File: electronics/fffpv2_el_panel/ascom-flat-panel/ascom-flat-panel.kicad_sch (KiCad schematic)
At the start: 17 parts, among them J1 Servo, J2 Conn_01x02, Q1 IRLZ34N, U1 XIAO-SAMD21-DIP, U2 TLC272, U4 LM317_TO-220

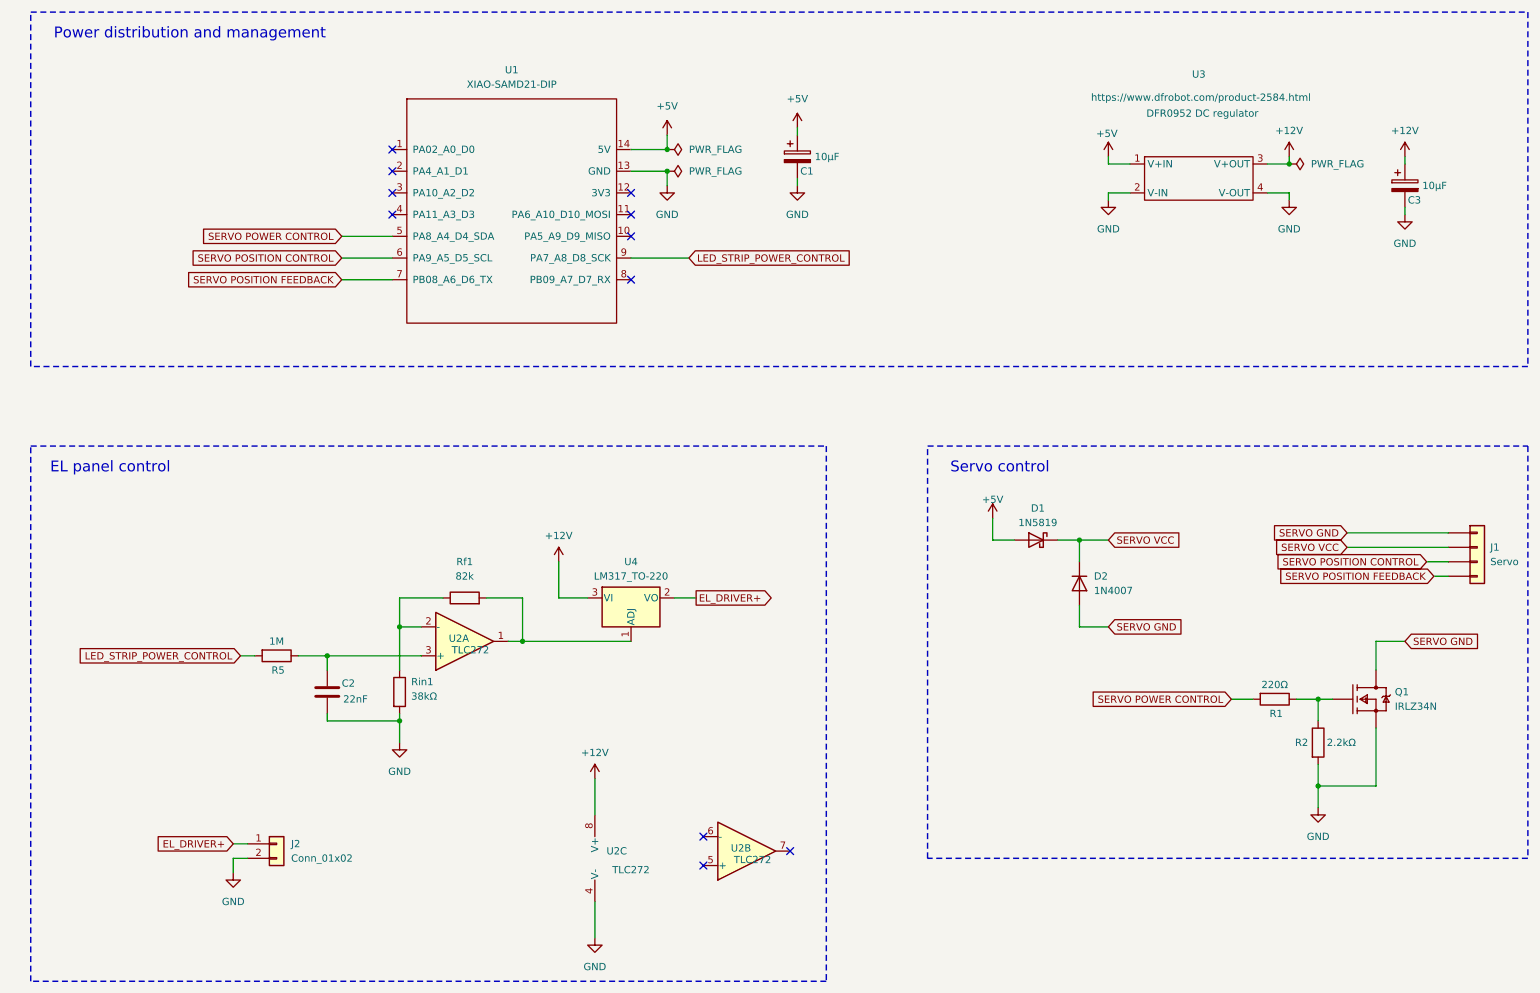
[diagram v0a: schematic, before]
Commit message: Updatong shcematics and PCB to use DAC for EL driver PWR ctrl
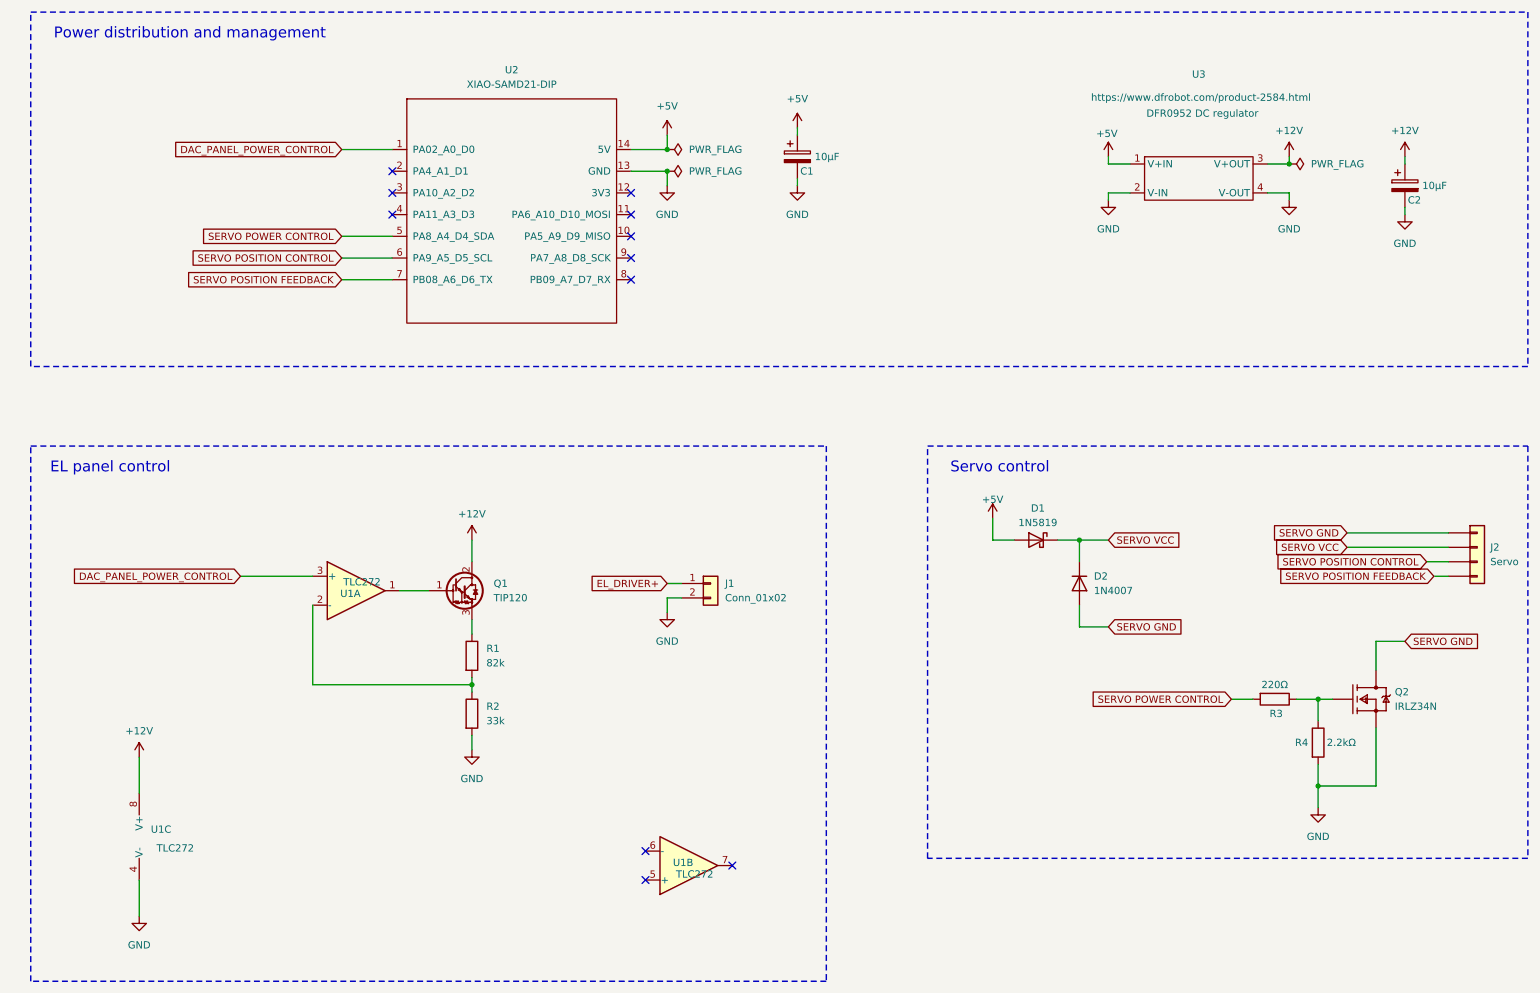
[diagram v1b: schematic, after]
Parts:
- removed C2: 22nF, Capacitor_THT:C_Disc_D3.0mm_W1.6mm_P2.50mm, symbol Device:C
- removed R5: 1M, Resistor_THT:R_Axial_DIN0207_L6.3mm_D2.5mm_P10.16mm_Horizontal, symbol Device:R
- removed Rf1: 82k, Resistor_THT:R_Axial_DIN0207_L6.3mm_D2.5mm_P10.16mm_Horizontal, symbol Device:R
- removed Rin1: 38kΩ, Resistor_THT:R_Axial_DIN0207_L6.3mm_D2.5mm_P10.16mm_Horizontal, symbol Device:R
- removed U4: LM317_TO-220, Package_TO_SOT_THT:TO-220-3_Vertical, symbol Regulator_Linear:LM317_TO-220
- added Q1: TIP120, Package_TO_SOT_THT:TO-220-3_Vertical, symbol Transistor_BJT:TIP120
- added R1: 82k, Resistor_THT:R_Axial_DIN0207_L6.3mm_D2.5mm_P10.16mm_Horizontal, symbol Device:R
- added R2: 33k, Resistor_THT:R_Axial_DIN0207_L6.3mm_D2.5mm_P10.16mm_Horizontal, symbol Device:R
- renumbered C3 to C2, J2 to J1, J1 to J2, Q1 to Q2, R1 to R3, R2 to R4, U2 to U1, U1 to U2
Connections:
- net +12V: now also Q1.2 (C)
- net GND: now also R2.2
- net at U1.1: now also Q1.1 (B)
- net DAC_PANEL_POWER_CONTROL: now reaches U1.3 (+)
- net DAC_PANEL_POWER_CONTROL: now also U2.1 (PA02_A0_D0)
- net at U1.2 (-): now also R1.2, R2.1
- net LED_STRIP_POWER_CONTROL: no longer names the net of U2.9 (PA7_A8_D8_SCK)
- new net: Q1.3 (E), R1.1
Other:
- moved on the sheet: J1, U1A, U1B, U1C

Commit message: Missing wiring the EL driver +
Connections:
- net EL_DRIVER+: now also Q1.3 (E), R1.1
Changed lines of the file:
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@@
+	)
+	(junction
+		(at 96.52 124.46)
+		(diameter 0)
+		(color 0 0 0 0)
 	)
 	(junction
@@
 	(wire
 		(pts
-			(xy 96.52 123.19) (xy 96.52 125.73)
+			(xy 96.52 123.19) (xy 96.52 124.46)
 		)
 		(stroke
@@
 	(wire
 		(pts
+			(xy 96.52 124.46) (xy 96.52 125.73)
+		)
+		(stroke
+			(width 0)
+			(type default)
+		)
+	)
+	(wire
+		(pts
 			(xy 73.66 55.88) (xy 82.55 55.88)
 		)
@@
 		(pts
 			(xy 255.27 142.24) (xy 255.27 152.4)
+		)
+		(stroke
+			(width 0)
+			(type default)
+		)
+	)
+	(wire
+		(pts
+			(xy 96.52 124.46) (xy 105.41 124.46)
 		)
 		(stroke
@@
 				(hide yes)
 			)
+		)
+	)
+	(global_label "EL_DRIVER+"
+		(shape input)
+		(at 105.41 124.46 0)
+		(fields_autoplaced yes)
+		(effects
+			(font
+				(size 1.27 1.27)
+			)
+			(justify left)
+		)
+		(property "Intersheetrefs" "${INTERSHEET_REFS}"
+			(at 119.7647 124.46 0)
+			(effects
+				(font
+					(size 1.27 1.27)
+				)
+				(justify left)
+				(hide yes)
+			)
